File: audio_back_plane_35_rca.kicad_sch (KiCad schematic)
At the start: 55 parts, among them J2 SJ3-35044A, J4 Conn_01x10, J5 Conn_02x10_Odd_Even, J6 SJ3-35044A, SW1 SW_SPST, SW2 SW_SPST, SW3 SW1, U1 ESP32-DevKitC - DEVKIT, U3 Teensy 4.1 - DEVKIT

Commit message: update
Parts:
- removed BYPASS1: jumper, project_fp:SolderJumper-2_P1.3mm_Bridged2Bar_RoundedPad1.0x1.5mm_OPEN, symbol Jumper:SolderJumper_2_Open
- removed EPROG1: header, project_fp:EPROG1_PinHeader_1x06_P2.54mm_Vertical, symbol Connector_Generic:Conn_01x06
- removed ESP_I1: header, project_fp:ESP_I2C_0_PinHeader_2x02_P2.54mm_Vertical, symbol Connector_Generic:Conn_02x02_Odd_Even
- removed GPI1: header, project_fp:GPI1_PinHeader_1x04_P2.54mm_Vertical, symbol Connector_Generic:Conn_01x04
- removed ILI1: ILI9341+XPT2046, project_fp:ILI9341_PinHeader_1x14_P2.54mm_Vertical, symbol project_lil_2:ILI9341_header
- removed ILI_VCC1: jumper, project_fp:SolderJumper-3_P1.3mm_Bridged2Bar12_Pad1.0x1.5mm_NumberLabels, symbol Jumper:SolderJumper_3_Bridged12
- removed J2, J6: SJ3-35044A, project_fp:SAMESKY_SJ3-35044A, symbol SJ3-35044A:SJ3-35044A
- removed J4: Conn_01x10, Connector_PinHeader_2.54mm:PinHeader_1x10_P2.54mm_Vertical, symbol Connector_Generic:Conn_01x10
- removed J5: Conn_02x10_Odd_Even, Connector_IDC:IDC-Header_2x10_P2.54mm_Vertical, symbol Connector_Generic:Conn_02x10_Odd_Even
- removed R15, R2, R3, R4, R5: 2.2k ohm - 2200 ohm, Resistor_THT:R_Axial_DIN0204_L3.6mm_D1.6mm_P5.08mm_Horizontal, symbol Device:R
- removed SW1, SW2: SW_SPST, project_fp:SW_Tactile_SPST_Angled_PTS645Vx39-2LFS, symbol Switch:SW_SPST
- removed USB_HOST1: header, project_fp:USB_OUT1, symbol project_lil_2:USB_header_1x5_2.54
- added D3, D4: SK6812_4020_SIDE_LED, project_fp:LED_4691, symbol SK6812_4020_SIDE_LED:SK6812_4020_SIDE_LED
- D1, D2: value WS2812B - COM-16347 -> HEADER; footprint Connector_PinHeader_1.00mm:PinHeader_1x04_P1.00mm_Vertical -> project_fp:PinHeader_1x04_P1.00mm_Vertical_WS2812_LED_mod; now not fitted
- G1, HPTRS1, HPTRS2, U1, U3, board_outline2: now not fitted
- R1, R10, R12, R13, R14, R17, R19, R20, R21, R6, R7, R8, R9: footprint Resistor_THT:R_Axial_DIN0204_L3.6mm_D1.6mm_P5.08mm_Horizontal -> project_fp:R_0805_2012Metric_Pad1.20x1.40mm_HandSolder
- SW3: value SW1 -> OS102011MA1QN1
- board_outline1: value board -> TAC5212 Module; now not fitted
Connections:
- net 3.3V: now also MIC2.2 (SELECT)
- net 34_RX8_RESET2: no longer U3.26 (34_RX8)
- net 5V: now also D3.2 (VDD), D4.2 (VDD)
- net GND: now also MIC1.2 (SELECT), D3.4 (GND), D4.4 (GND)
- net at SW3.2 (C): now also HPTRS2.2; no longer HPTRS2.5
- net at board_outline1.21 (OUTP): now also HPTRS1.5; no longer HPTRS1.2
- net at board_outline1.25 (OUT2P): now also HPTRS1.2; no longer HPTRS1.5
- net at board_outline1.29 (IN1P): now also HPTRS2.5; no longer HPTRS2.2
- net at D2.1 (Pin_1), R17.1: now also D4.1 (DIN)
- net at D1.1 (Pin_1), R13.1: now also D3.1 (DIN)
- net ESP32_IO21_SDA: no longer names the net of U1.33 (GPIO21)
- net ESP32_IO22_SCL: no longer names the net of U1.36 (GPIO22)
- net MIDI_RX: no longer names the net of U3.2 (0_RX1_CRX2_CS1)
- net MIDI_TX_T: no longer names the net of U3.3 (1_TX1_CTX2_MISO1)
- net T_BUTTON1: no longer names the net of U3.16 (24_A10_TX6_SCL2)
- net T_BUTTON2: no longer names the net of U3.17 (25_A11_RX6_SDA2)
- new net: MIC1.4 (LRCLK-WS-FS), MIC2.4 (LRCLK-WS-FS), board_outline1.40 (GPIO1)
- now unconnected: MIC1.4 (LRCLK-WS-FS), MIC2.4 (LRCLK-WS-FS)
- no-connect marks 8 -> 6
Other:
- moved on the sheet: C8, R13, R17, SW3, USBA1

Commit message: update
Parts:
- added D10, D11, D5, D6, D7, D8: SK6812, project_fp:LED_SK6812_EC15_1.5x1.5mm, symbol SK6812_4020_SIDE_LED:SK6812_REVERSE_MOUNT
- added D9: SK6812, project_fp:LED_SK6812, symbol SK6812:SK6812
- added SW1: RotaryEncoder_Switch_MP, project_fp:RotaryEncoder_Alps_EC11E_Vertical_H20mm, symbol Device:RotaryEncoder_Switch_MP
- added SW2, SW4, SW5, SW6: TL1105WF160Q - 3.15mm actuator, project_fp:Tactile_Switch_4.54.5MM, symbol Switch:SW_SPST
- D3, D4: value SK6812_4020_SIDE_LED -> SK6812; footprint project_fp:LED_4691 -> project_fp:LED_SK6812_EC15_1.5x1.5mm; symbol SK6812_4020_SIDE_LED:SK6812_4020_SIDE_LED -> SK6812_4020_SIDE_LED:SK6812_REVERSE_MOUNT
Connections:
- net 5V: now also D3.1 (VDD), D4.1 (VDD), D5.1 (VDD), D6.1 (VDD); no longer D3.2 (VDD), D4.2 (VDD)
- net GND: now also D3.3 (GND), D4.3 (GND), D5.3 (GND); no longer D3.4 (GND), D4.4 (GND)
- net at D2.1 (Pin_1), R17.1: now also D4.4 (DIN); no longer D4.1 (DIN)
- net at D1.1 (Pin_1), R13.1: now also D3.4 (DIN); no longer D3.1 (DIN)
- net T_BUTTON1: now reaches U3.16 (24_A10_TX6_SCL2)
- net T_BUTTON1: now also SW2.1 (A), SW5.1 (A)
- net T_BUTTON2: now reaches U3.17 (25_A11_RX6_SDA2)
- net T_BUTTON2: now also SW4.1 (A), SW6.1 (A)
- new net: MIC1.4 (LRCLK-WS-FS), MIC2.4 (LRCLK-WS-FS), board_outline1.40 (GPIO1)
- new net: D4.2 (DOUT), D5.4 (DIN)
- new net: D3.2 (DOUT), D6.4 (DIN)
- now unconnected: MIC1.4 (LRCLK-WS-FS), MIC2.4 (LRCLK-WS-FS)
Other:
- note added: "SWITCHES"

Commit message: update
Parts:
- added SW7: TL1105WF160Q - 3.15mm actuator, project_fp:Tactile_Switch_4.54.5MM, symbol Switch:SW_SPST
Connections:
- net T_BUTTON2: now also SW7.1 (A)
- new net: MIC1.4 (LRCLK-WS-FS), MIC2.4 (LRCLK-WS-FS), board_outline1.40 (GPIO1)
- now unconnected: MIC1.4 (LRCLK-WS-FS), MIC2.4 (LRCLK-WS-FS)
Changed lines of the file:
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@@
 		)
 	)
+	(global_label "T_BUTTON2"
+		(shape input)
+		(at 781.05 778.51 180)
+		(fields_autoplaced yes)
+		(effects
+			(font
+				(size 1.27 1.27)
+			)
+			(justify right)
+		)
+		(property "Intersheetrefs" "${INTERSHEET_REFS}"
+			(at 768.457 778.51 0)
+			(effects
+				(font
+					(size 1.27 1.27)
+				)
+				(justify right)
+				(hide yes)
+			)
+		)
+	)
 	(global_label "GND"
 		(shape input)
@@
 	)
 	(symbol
+		(lib_id "Switch:SW_SPST")
+		(at 786.13 778.51 0)
+		(unit 1)
+		(exclude_from_sim no)
+		(in_bom yes)
+		(on_board yes)
+		(dnp no)
+		(property "Reference" "SW7"
+			(at 786.13 773.43 0)
+			(effects
+				(font
+					(size 1.27 1.27)
+				)
+			)
+		)
+		(property "Value" "TL1105WF160Q - 3.15mm actuator"
+			(at 784.86 788.67 0)
+			(effects
+				(font
+					(size 1.27 1.27)
+				)
+			)
+		)
+		(property "Footprint" "project_fp:Tactile_Switch_4.54.5MM"
+			(at 786.13 778.51 0)
+			(effects
+				(font
+					(size 1.27 1.27)
+				)
+				(hide yes)
+			)
+		)
+		(property "Datasheet" "~"
+			(at 786.13 778.51 0)
+			(effects
+				(font
+					(size 1.27 1.27)
+				)
+				(hide yes)
+			)
+		)
+		(property "Description" ""
+			(at 786.13 778.51 0)
+			(effects
+				(font
+					(size 1.27 1.27)
+				)
+				(hide yes)
+			)
+		)
+		(pin "1"
+		)
+		(pin "2"
+		)
+		(instances
+			(project "audio_back_plane_35_rca"
+				(path "/6a0ff39d-771d-410f-9e7c-006586d81d16"
+					(reference "SW7")
+					(unit 1)
+				)
+			)
+		)
+	)
+	(symbol
 		(lib_id "power:GND")
 		(at 527.05 601.98 0)
@@
 	)
 	(symbol
-		(lib_name "lib_sch:SPH0645LM4H")
 		(lib_id "lib_sch:SPH0645LM4H")
 		(at 815.34 575.31 0)
@@
 	)
 	(symbol
-		(lib_name "lib_sch:SPH0645LM4H")
 		(lib_id "lib_sch:SPH0645LM4H")
 		(at 815.34 551.18 0)

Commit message: added tft touchscreen
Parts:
- removed SW3: OS102011MA1QN1, Button_Switch_THT:SW_Slide_SPDT_Angled_CK_OS102011MA1Q, symbol TEENSY_4.0_PCM5242_TPA6120A2-rescue:SolderJumper_3_Bridged12-project_lib
- added D12: SK6812, project_fp:LED_SK6812_EC15_1.5x1.5mm, symbol SK6812_4020_SIDE_LED:SK6812_REVERSE_MOUNT
- added HPTRS3: 3.5MM JACK, project_fp:35RAPC3BH3, symbol 35RAPC3BH3:AudioJack3_SwitchTR
- added J1: Conn_02x10_Odd_Even, Connector_IDC:IDC-Header_2x10_P2.54mm_Vertical, symbol Connector_Generic:Conn_02x10_Odd_Even
- added J2: Conn_02x10_Odd_Even, Connector_IDC:IDC-Header_2x10_P2.54mm_Vertical_SMD, symbol Connector_Generic:Conn_02x10_Odd_Even
- added U2: TFT_320x240, project_fp:TFT-320x240, symbol tft_320x240:TFT_320x240
- HPTRS1: Label PHONE -> OUT
- HPTRS2: Label PHONE -> IN1; now fitted
- U3: footprint project_fp:Teensy41_mod2 -> project_fp:Teensy41_mod
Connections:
- net GND: now also HPTRS3.1
- net at board_outline1.33 (IN2P): now also HPTRS3.5
- net at HPTRS2.2: now also board_outline1.31 (IN1M), HPTRS3.3
- net at board_outline1.35 (IN2M): now also HPTRS3.2
- new net: MIC1.4 (LRCLK-WS-FS), MIC2.4 (LRCLK-WS-FS), board_outline1.40 (GPIO1)
- now unconnected: MIC1.4 (LRCLK-WS-FS), MIC2.4 (LRCLK-WS-FS)
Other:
- note added: "TWO INPUT MODES IN1: Stereo/Mono Balanced IN2 INSERTED = Dual Balanced Inputs"
- moved on the sheet: HPTRS1

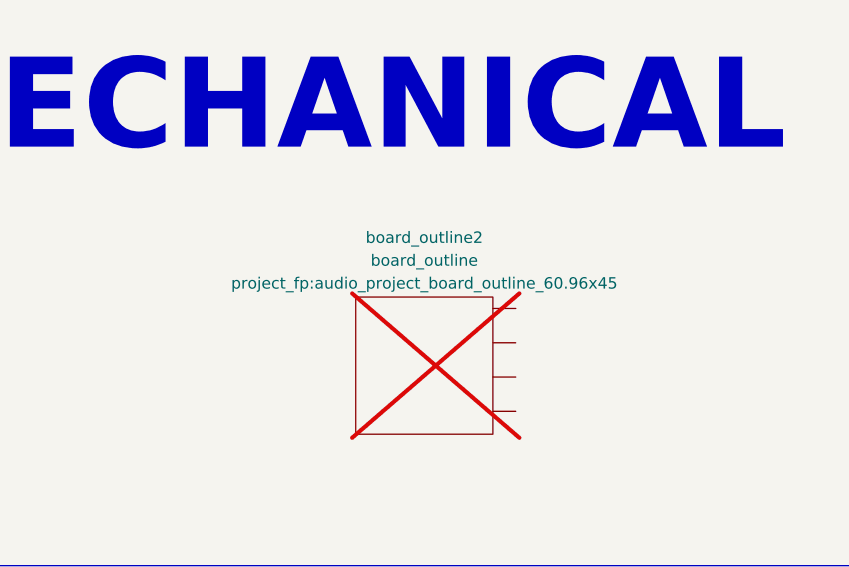
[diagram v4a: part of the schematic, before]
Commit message: added touchscreen
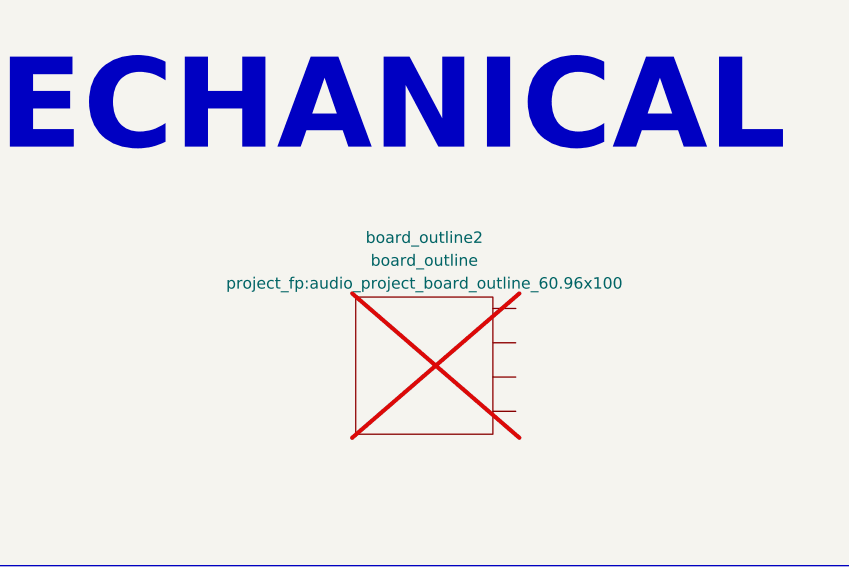
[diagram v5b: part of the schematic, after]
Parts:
- board_outline2: footprint project_fp:audio_project_board_outline_60.96x45 -> project_fp:audio_project_board_outline_60.96x100
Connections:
- new net: MIC1.4 (LRCLK-WS-FS), MIC2.4 (LRCLK-WS-FS), board_outline1.40 (GPIO1)
- now unconnected: MIC1.4 (LRCLK-WS-FS), MIC2.4 (LRCLK-WS-FS)
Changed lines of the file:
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@@
 			)
 		)
-		(property "Footprint" "project_fp:audio_project_board_outline_60.96x45"
+		(property "Footprint" "project_fp:audio_project_board_outline_60.96x100"
 			(at 830.58 694.436 0)
 			(effects

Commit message: update
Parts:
- removed J1: Conn_02x10_Odd_Even, Connector_IDC:IDC-Header_2x10_P2.54mm_Vertical, symbol Connector_Generic:Conn_02x10_Odd_Even
- removed J2: Conn_02x10_Odd_Even, Connector_IDC:IDC-Header_2x10_P2.54mm_Vertical_SMD, symbol Connector_Generic:Conn_02x10_Odd_Even
- added HPTRS2: 3.5MM JACK, project_fp:35RAPC3BH3, symbol 35RAPC3BH3:AudioJack3_SwitchTR
- added IC1: TMUX4053DYYR, SOP50P326X110-16N, symbol SamacSys_Parts:TMUX4053DYYR_MOD
- added IC2: SN74LVC245ARGYR, SN74LVC541ARGYR, symbol SamacSys_Parts:SN74LVC245ARGYR
- added ILI1: ILI9341+XPT2046, project_fp:ILI9341_PinHeader_1x14_P2.54mm_Vertical, symbol project_lil_2:ILI9341_header
- added ILI_VCC1: jumper, project_fp:SolderJumper-3_P1.3mm_Bridged2Bar12_Pad1.0x1.5mm_NumberLabels, symbol Jumper:SolderJumper_3_Bridged12
- added J3, J4: header, project_fp:PinHeader_1x02_P2.54mm_Vertical_W_CUT, symbol Connector_Generic:Conn_02x02_Odd_Even
- added R16, R17: 0 ohm, project_fp:R_0805_2012Metric_Pad1.20x1.40mm_HandSolder, symbol Device:R
- added R18, R19, R20, R21, R22, R23, R24, R25: 49.9 ohm, project_fp:R_0805_2012Metric_Pad1.20x1.40mm_HandSolder, symbol Device:R
- added R6: 10k, project_fp:R_0805_2012Metric_Pad1.20x1.40mm_HandSolder, symbol Device:R
- added R9: 100 ohm, project_fp:R_0805_2012Metric_Pad1.20x1.40mm_HandSolder, symbol Device:R
- added TDM1, TDM2: header, project_fp:T-DSP_Expansion_Header_2x10_ALT_GND, symbol project_lil_2:TDM_HEADER_Conn_02x10_Odd_Even
- HPTRS1: now fitted
- U1: renamed from U3; footprint project_fp:Teensy41_mod -> project_fp:Teensy41_mod2
- U3: renamed from U2; now not fitted; now left out of the parts list
- renumbered C3 to C1, C9 to C2, C5 to C3, C1 to C4, C10 to C5, C2 to C6, C8 to C7, D12 to D10, D9 to D12, D3 to D2, D6 to D3, D2 to D4, D4 to D5, D5 to D6, D10 to D9, HPTRS2 to HPTRS3, HPTRS3 to HPTRS4, R6 to R1, R14 to R10, R17 to R11, R1 to R12, R19 to R13, R20 to R14, R21 to R15, R7 to R2, R8 to R3, R9 to R4, R10 to R5, R13 to R7, R12 to R8, SW4 to SW3, SW7 to SW4, U1 to U2
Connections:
- net 12V: now also TDM1.5 (12V), TDM2.5 (12V)
- net 3.3V: now also IC1.16 (VDD), IC1.6 (~{EN}), ILI1.8 (LED_(3.3V)), ILI_VCC1.1 (A), R6.1
- net 32_OUT1B: now also R9.1
- net 34_RX8_RESET2: now also TDM1.2 (HELD_LOW), TDM2.2 (HELD_LOW)
- net 35_TX8_RESET: now also TDM1.1 (HELD_HIGH), TDM2.1 (HELD_HIGH)
- net 5V: now also ILI_VCC1.3 (B), TDM1.3 (5V), TDM2.3 (5V)
- net GND: now also HPTRS2.1, IC1.7 (VSS), IC1.8 (GND), ILI1.2 (GND), TDM1.10 (GND), TDM1.12 (GND), TDM1.14 (GND), TDM1.16 (GND), TDM1.18 (GND), TDM1.20 (GND), TDM1.6 (GND), TDM1.8 (GND), TDM2.10 (GND), TDM2.12 (GND), TDM2.14 (GND), TDM2.16 (GND), TDM2.18 (GND), TDM2.20 (GND), TDM2.6 (GND), TDM2.8 (GND)
- net at U2.23 (*MTDO/GPIO15/ADC2_CH3): now also ILI1.3 (CS)
- net at U2.24 (ADC2_CH2/*GPIO2): now also ILI1.5 (DC)
- net at U2.26 (ADC2_CH0/GPIO4): now also ILI1.4 (RESET)
- net at U2.30 (GPIO18): now also ILI1.10 (T_CLK(SCK)), ILI1.7 (SCK)
- net at U2.31 (GPIO19): now also ILI1.11 (T_DO(MISO))
- net at U2.37 (GPIO23): now also ILI1.12 (T_DIN(MOSI)), ILI1.6 (SDI(MOSI))
- net at U2.7 (32K_XP/GPIO32/ADC1_CH4): now also ILI1.13 (T_CS)
- net IN2_JACK_DETECT: now reaches HPTRS4.4
- net IN2_JACK_DETECT: now also U1.18 (26_A12_MOSI1), R6.2
- net at HPTRS1.5, board_outline1.21 (OUTP): now also IC1.1 (S2B)
- net at board_outline1.23 (OUT1M): now also IC1.12 (S1A)
- net at board_outline1.25 (OUT2P): now also IC1.13 (S1B), IC1.2 (S2A), IC1.5 (S3A); no longer HPTRS1.2
- net at board_outline1.27 (OUT2M): now also IC1.3 (S3B)
- net at U1.24 (32_OUT1B): now also R9.2
- new net: R24.1, TDM1.19 (MCLK)
- new net: ILI1.1 (VCC_(5V)), ILI_VCC1.2 (C)
- new net: R20.1, TDM1.11 (BCLK)
- new net: R22.1, TDM1.13 (LRCK)
- new net: R16.1, TDM1.7 (DSP_DATA_IN)
- new net: R18.1, TDM1.9 (DSP_DATA_OUT)
- new net: MIC1.4 (LRCLK-WS-FS), MIC2.4 (LRCLK-WS-FS), board_outline1.40 (GPIO1)
- new net: J3.1 (Pin_1), R16.2
- new net: J3.3 (Pin_3), R18.2
- new net: R21.1, TDM2.11 (BCLK)
- new net: HPTRS1.2, IC1.14 (D1)
- new net: HPTRS2.5, IC1.15 (D2)
- new net: HPTRS2.2, IC1.4 (D3)
- new net: R25.1, TDM2.19 (MCLK)
- new net: R23.1, TDM2.13 (LRCK)
- new net: R17.1, TDM2.7 (DSP_DATA_IN)
- new net: R19.1, TDM2.9 (DSP_DATA_OUT)
- new net: J4.3 (Pin_3), R19.2
- new net: J4.1 (Pin_1), R17.2
- new net 7_OUT1A+: J3.4 (Pin_4), J4.4 (Pin_4)
- new net 8_IN1+: J3.2 (Pin_2), J4.2 (Pin_2)
- new net BCLK1+: R20.2, R21.2
- new net LRCK1+: R22.2, R23.2
- new net MCLK1+: R24.2, R25.2
- new net SCL_C: TDM1.17 (SCL)
- new net SCL_D: TDM2.17 (SCL)
- new net SDA_C: TDM1.15 (SDA)
- new net SDA_D: TDM2.15 (SDA)
- new net SYSTEM_EN: TDM1.4 (GND), TDM2.4 (GND)
- now unconnected: MIC1.4 (LRCLK-WS-FS), MIC2.4 (LRCLK-WS-FS)
- no-connect marks 6 -> 8

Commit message: update
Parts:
- removed D12: SK6812, project_fp:LED_SK6812, symbol SK6812:SK6812
- removed J4: header, project_fp:PinHeader_1x02_P2.54mm_Vertical_W_CUT, symbol Connector_Generic:Conn_02x02_Odd_Even
- removed R17: 0 ohm, project_fp:R_0805_2012Metric_Pad1.20x1.40mm_HandSolder, symbol Device:R
- removed R19: 49.9 ohm, project_fp:R_0805_2012Metric_Pad1.20x1.40mm_HandSolder, symbol Device:R
- removed TDM2: header, project_fp:T-DSP_Expansion_Header_2x10_ALT_GND, symbol project_lil_2:TDM_HEADER_Conn_02x10_Odd_Even
- added Brd1: SSD1306, project_fp:Adafruit_SSD1306_I2C_ONLY, symbol SSD1306-128x64_OLED:SSD1306
- added CC1, CC2: 5.1k, project_fp:R_0805_2012Metric_Pad1.20x1.40mm_HandSolder, symbol Device:R
- added D12, D13, D14, D15, D16, D17, D18, D19, D20, D21, D22: SK6812, project_fp:LED_SK6812_EC15_1.5x1.5mm, symbol SK6812_4020_SIDE_LED:SK6812_REVERSE_MOUNT
- added G2: jumper, project_fp:SolderJumper-2_P1.3mm_Open_TrianglePad1.0x1.5mm, symbol Device:R
- added IC3: TMUX4052BQBR, TMUX4052BQBR, symbol project_sch:TMUX4052BQBR_MOD
- added IC4: TMUX4053BQBR, TMUX4053BQBR, symbol SamacSys_Parts:TMUX4053BQBR
- added IC5: TMUX4053DYYR, SOP50P326X110-16N, symbol SamacSys_Parts:TMUX4053DYYR_MOD
- added Q1, Q2: IRLML6344TRPBF, SOT95P237X112-3N, symbol SamacSys_Parts:IRLML6344TRPBF
- added R24: 6.8k, project_fp:R_0805_2012Metric_Pad1.20x1.40mm_HandSolder, symbol Device:R
- added U4: EN11-HSM1AF15, project_fp:EN11-HSM_TTE, symbol EN11_HSM1AF15:EN11-HSM1AF15
- added USBB1: USB B Device (Optional) - B1HSxx, project_fp:USB_B_OST_USB-B1HSxx_Horizontal, symbol project_lil_2:USB3_A
- added USBC1: USB C Device - USB4085-GF-A, project_fp:GCT_USB4085-GF-A_REVA4, symbol project_lil_2:USB4085-GF-A_REVA4
- added USB_IN1, USB_THRU1: header, project_fp:USB_IN1, symbol project_lil_2:USB_header_1x5_2.54
- R21, R23, R25: value 49.9 ohm -> 6.8k; Digikey (none) -> ERJ-PA2F2211X-ND; Manufacturer (none) -> YAGEO; Manufacturer_Part_Number (none) -> RC0805DR-072K2L
- board_outline2: footprint project_fp:audio_project_board_outline_60.96x100 -> project_fp:audio_project_board_outline_100x75
- renumbered J3 to J1, R18 to R17, R20 to R18, R22 to R19, R24 to R20
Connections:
- net 5V: now also D10.1 (VDD), D11.1 (VDD), D7.1 (VDD), D8.1 (VDD), D9.1 (VDD), D12.1 (VDD), D13.1 (VDD), D14.1 (VDD), D15.1 (VDD), D16.1 (VDD), D17.1 (VDD), D18.1 (VDD), D19.1 (VDD), D20.1 (VDD), D21.1 (VDD), D22.1 (VDD), USB_THRU1.1 (5V)
- net BCLK1+: no longer R21.2
- net DEVICE_D1+: now also USBB1.3 (D+), USBC1.A6 (DP1), USB_IN1.3 (D1+), USB_THRU1.3 (D1+)
- net DEVICE_D1-: now also USBB1.2 (D-), USBC1.A7 (DN1), USB_IN1.2 (D1-), USB_THRU1.2 (D1-)
- net GND: now also D10.3 (GND), D11.3 (GND), D3.3 (GND), D7.3 (GND), D8.3 (GND), D9.3 (GND), CC1.1, CC2.1, D12.3 (GND), D13.3 (GND), D14.3 (GND), D15.3 (GND), D16.3 (GND), D17.3 (GND), D18.3 (GND), D19.3 (GND), D20.3 (GND), D21.3 (GND), D22.3 (GND), G2.1, USBB1.4 (GND), USBC1.A1 (GND), USBC1.A12 (GND), USBC1.B1 (GND), USBC1.B12 (GND), USB_IN1.4 (GND), USB_THRU1.4 (GND)
- net LRCK1+: no longer R23.2
- net MCLK1+: no longer R25.2
- net at D7.2 (DOUT): now also D8.4 (DIN)
- net at D7.4 (DIN): now also D6.2 (DOUT)
- net at HPTRS4.2, board_outline1.35 (IN2M): now also R21.2
- net at HPTRS3.2, HPTRS4.3, board_outline1.31 (IN1M): now also R24.2
- net at HPTRS4.5, board_outline1.33 (IN2P): now also R23.2
- net at D11.2 (DOUT): now also D12.4 (DIN)
- net at D11.4 (DIN): now also D8.2 (DOUT)
- net at IC1.1 (S2B), board_outline1.21 (OUTP): now also IC4.8 (GND_1); no longer HPTRS1.5
- net at HPTRS3.5, board_outline1.29 (IN1P): now also R25.2
- net at D10.4 (DIN): now also D9.2 (DOUT)
- net at D9.4 (DIN): now also D3.2 (DOUT)
- net at R21.1: now also R23.1, Q1.2 (S)
- net at R25.1: now also Q2.2 (S), R24.1
- new net: CC1.2, USBC1.A5 (CC1)
- new net: HPTRS1.5, IC4.9 (SEL3)
- new net: D15.2 (DOUT), D16.4 (DIN)
- new net: D14.2 (DOUT), D15.4 (DIN)
- new net: D18.2 (DOUT), D19.4 (DIN)
- new net: D17.2 (DOUT), D18.4 (DIN)
- new net: D16.2 (DOUT), D17.4 (DIN)
- new net: D13.2 (DOUT), D14.4 (DIN)
- new net: D12.2 (DOUT), D13.4 (DIN)
- new net: MIC1.4 (LRCLK-WS-FS), MIC2.4 (LRCLK-WS-FS), board_outline1.40 (GPIO1)
- new net: CC2.2, USBC1.B5 (CC2)
- new net: D19.2 (DOUT), D20.4 (DIN)
- new net: D20.2 (DOUT), D21.4 (DIN)
- new net: D21.2 (DOUT), D22.4 (DIN)
- new net 48v: Q1.3 (D), Q2.3 (D)
- new net 5VIN2: USBB1.1 (VBUS), USBC1.A4 (VBUS), USBC1.A9 (VBUS), USBC1.B4 (VBUS), USBC1.B9 (VBUS), USB_IN1.1 (5V)
- new net PHANTOM_SW1: Q2.1 (G)
- new net PHANTOM_SW2: Q1.1 (G)
- new net USB_SHIELD: G2.2, USBB1.5 (SHIELD), USBC1.S1 (SHELL), USBC1.S2 (SHELL), USBC1.S3 (SHELL), USBC1.S4 (SHELL), USB_IN1.5 (SHIELD), USB_THRU1.5 (SHIELD)
- now unconnected: MIC1.4 (LRCLK-WS-FS), MIC2.4 (LRCLK-WS-FS)
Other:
- note added: "5VIN to Current Limiter/Switch"
- note added: "Post Current Limiter/Switch"
- note added: "USB B Option"
- note added: "USB C DEVICE PORT"
- note added: "USB C Option"
- note added: "https://idyl.io/how-to-add-usb-type-c-micro-usb-replacement/?amp"
- moved on the sheet: C2, C5, HPTRS1, HPTRS2, HPTRS3, HPTRS4, IC1, IC2, J1, MIC1, MIC2, R16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

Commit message: update
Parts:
- added D23: LED, symbol Device:LED
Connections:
- new net: MIC1.4 (LRCLK-WS-FS), MIC2.4 (LRCLK-WS-FS), board_outline1.40 (GPIO1)
- now unconnected: MIC1.4 (LRCLK-WS-FS), MIC2.4 (LRCLK-WS-FS)
